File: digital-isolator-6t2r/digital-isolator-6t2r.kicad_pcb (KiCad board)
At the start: 2 copper layers, 47.1 x 42 mm, 28 parts, among them J1 Conn_02x08_Odd_Even, J2 Conn_02x08_Odd_Even, U1 ADuM1401xRW, U2 ADuM1401xRW

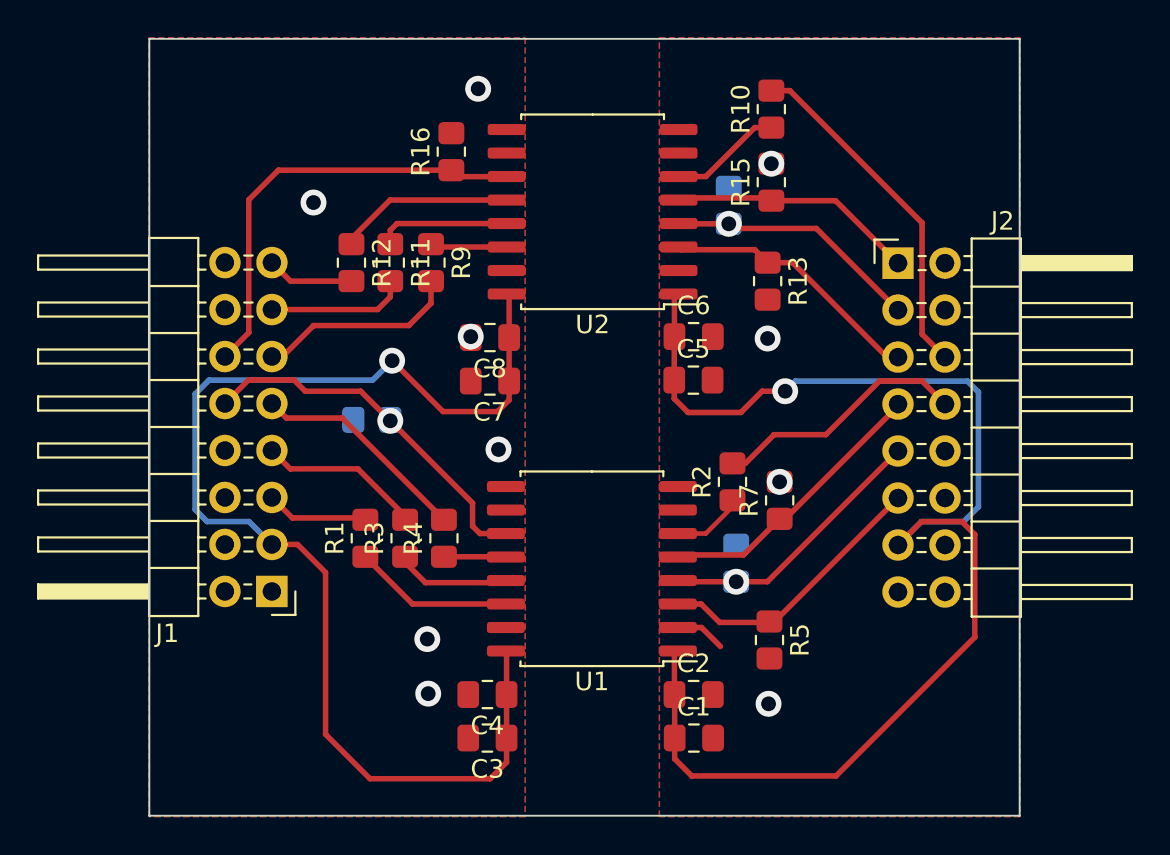
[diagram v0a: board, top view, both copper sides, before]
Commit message: Copper tracks as edge cuts to digital iso 6t2r for in-house fab
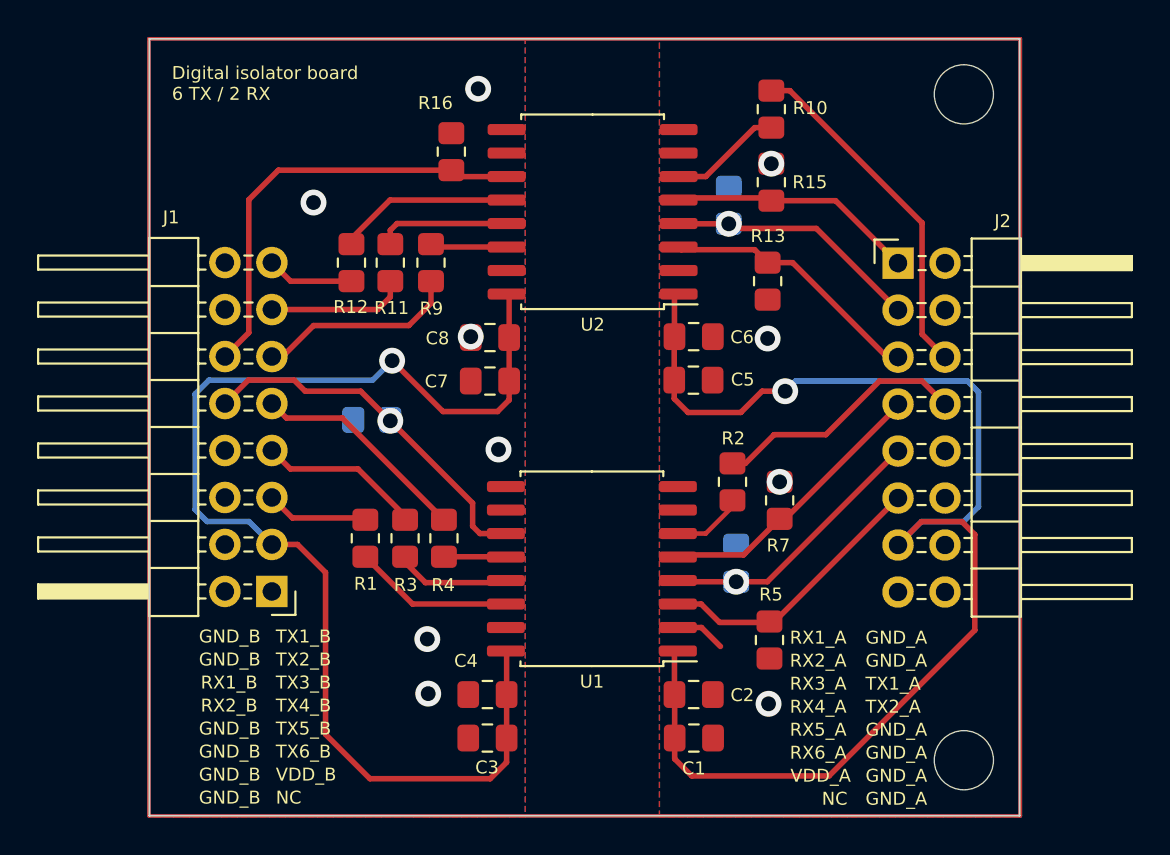
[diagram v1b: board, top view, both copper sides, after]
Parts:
- added H1: MountingHole, MountingHole:MountingHole_3.2mm_M3, F.Cu at (119.8, 70.7)
- added H2: MountingHole, MountingHole:MountingHole_3.2mm_M3, F.Cu at (119.8, 34.7)
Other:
- board text added: "Digital isolator board 6 TX / 2 RX"
- board text added: "GND_A"
- board text added: "GND_B"
- board text added: "NC"
- board text added: "RX1_A"
- board text added: "RX1_B"
- board text added: "RX2_A"
- board text added: "RX2_B"
- board text added: "RX3_A"
- board text added: "RX4_A"
- board text added: "RX5_A"
- board text added: "RX6_A"
- board text added: "TX1_A"
- board text added: "TX1_B"
- board text added: "TX2_A"
- board text added: "TX2_B"
- board text added: "TX3_B"
- board text added: "TX4_B"
- board text added: "TX5_B"
- board text added: "TX6_B"
- board text added: "VDD_A"
- board text added: "VDD_B"

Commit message: Added pull up resistors to dig iso 6t2r board
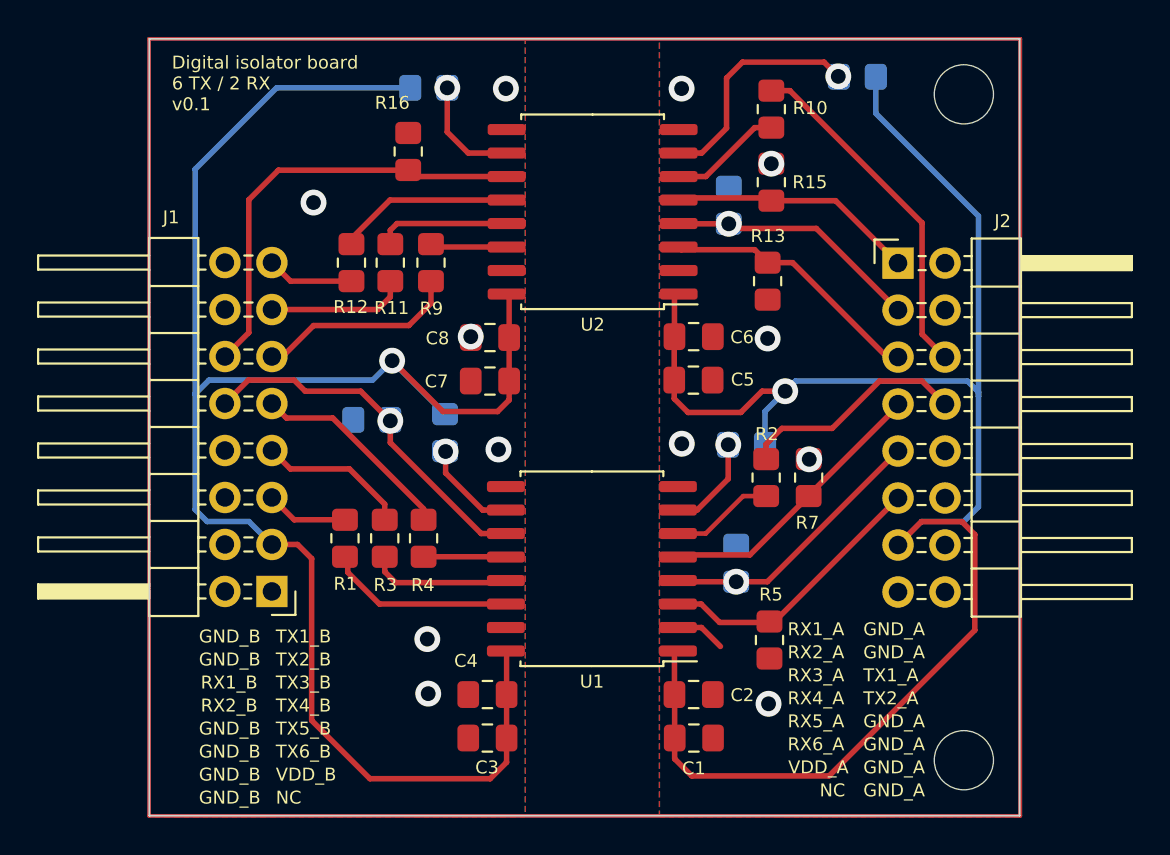
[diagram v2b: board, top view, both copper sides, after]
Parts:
- added R17: 100k, Resistor_SMD:R_0805_2012Metric_Pad1.20x1.40mm_HandSolder, B.Cu at (108.0, 53.6)
- added R18: 100k, Resistor_SMD:R_0805_2012Metric_Pad1.20x1.40mm_HandSolder, B.Cu at (91.7, 53.0)
- added R19: 100k, Resistor_SMD:R_0805_2012Metric_Pad1.20x1.40mm_HandSolder, B.Cu at (114.0, 33.8)
- added R20: 100k, Resistor_SMD:R_0805_2012Metric_Pad1.20x1.40mm_HandSolder, B.Cu at (90.8, 34.4)
- moved R16 2.33 mm to (89.7, 37.8)
- moved R7 1.99 mm to (111.4, 55.4)
- moved R2 1.83 mm to (109.1, 55.4)
- moved R1 1.10 mm to (86.3, 58.7)
- moved R4 1.10 mm to (90.5, 58.7)
- moved R3 1.10 mm to (88.5, 58.7)
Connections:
- U1 pad 10: unconnected-(U1-Pad10) -> Net-(R18-Pad2)
- U1 pad 7: unconnected-(U1-Pad7) -> Net-(R17-Pad1)
- U2 pad 10: unconnected-(U2-Pad10) -> Net-(R20-Pad2)
- U2 pad 7: unconnected-(U2-Pad7) -> Net-(R19-Pad1)
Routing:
- net VDDB: track 65.6 -> 95.2 mm
- net VDDA: track 70.8 -> 93.7 mm
- net Net-(R19-Pad1): track 0.00 -> 12.6 mm, vias 0 -> 1
- net Net-(R20-Pad2): track 0.00 -> 6.07 mm, vias 0 -> 1
- net Net-(R17-Pad1): track 0.00 -> 5.27 mm, vias 0 -> 1
- net Net-(R18-Pad2): track 0.00 -> 5.25 mm, vias 0 -> 1
- net /adum241x1/TX1_A': track 3.90 -> 5.61 mm
- net /adum241x1/TX1_B': track 8.66 -> 10.2 mm
- net /TX2_A: track 13.8 -> 12.4 mm
- net /adum241x1/TX2_B': track 6.25 -> 7.65 mm
- net /adum241x1/TX3_B': track 3.36 -> 4.46 mm
- net /TX4_B: track 11.9 -> 11.1 mm
- net /TX5_B: track 8.87 -> 8.14 mm
- net /TX6_B: track 5.01 -> 4.45 mm
- net GNDA: vias 4 -> 6
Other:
- board text added: "Digital isolator board 6 TX / 2 RX v0.1"
- board text removed: "Digital isolator board 6 TX / 2 RX"
